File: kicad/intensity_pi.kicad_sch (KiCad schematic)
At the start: 65 parts, among them J1 Input A, J2 Input B / Setpoint, J3 Monitor, J4 Output, J7 select 1, SW1 SW_DPDT_x2, SW2 SW_DPDT_x2, SW3 SW_DPDT_x2, SW4 SW_SP4T, SW5 SW_DPDT_x2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

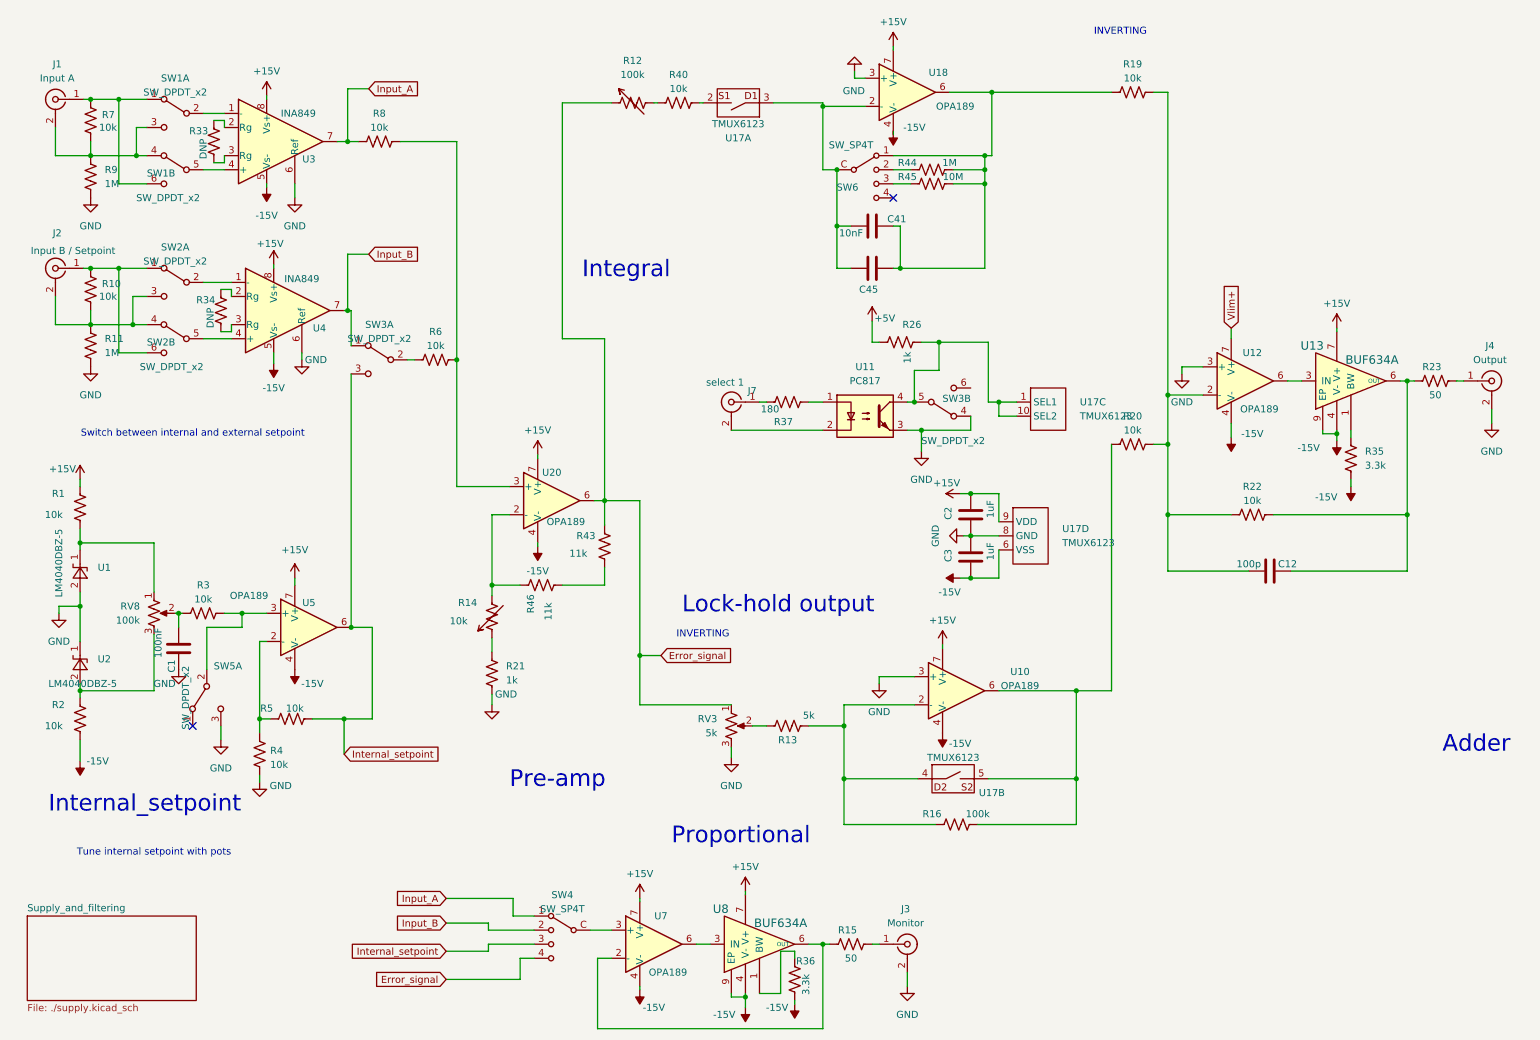
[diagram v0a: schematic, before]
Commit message: Updated Schematic, removed sw1,2,3a,4, have to fix 3a for zero offset switch
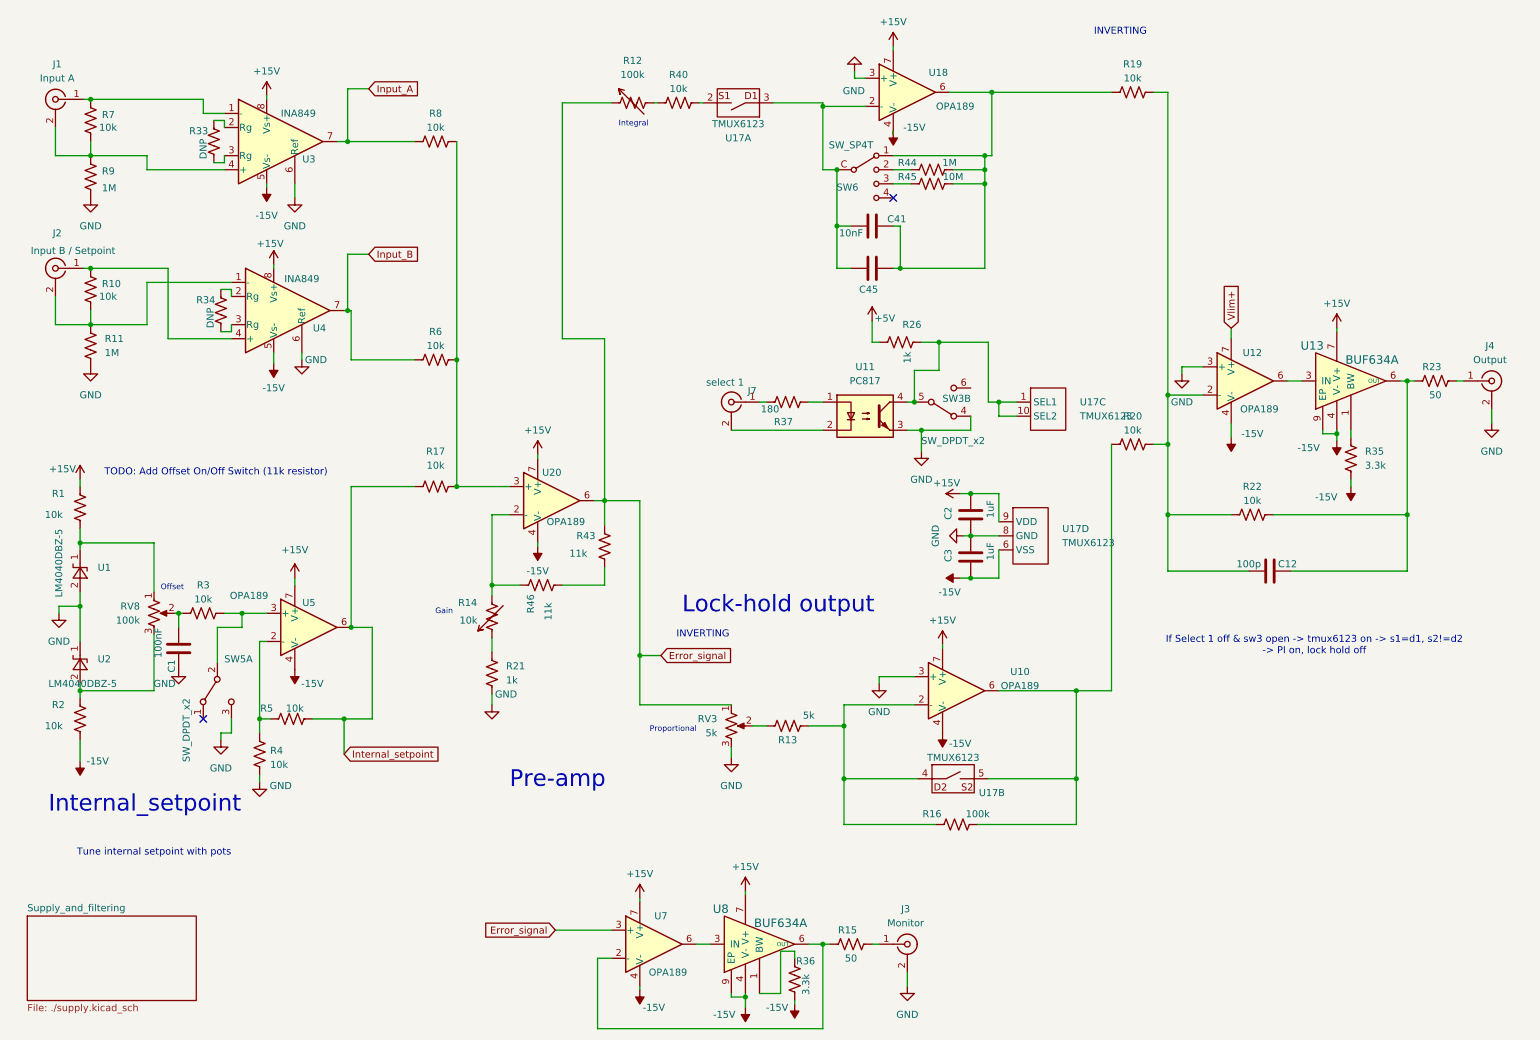
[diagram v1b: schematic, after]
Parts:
- removed SW1, SW2: SW_DPDT_x2, lib:MHS222, symbol local_lib:SW_DPDT_x2
- removed unit 1 of SW3
- removed SW4: SW_SP4T, lib:SLB1470, symbol local_lib:SW_SP4T
- added R17: 10k, symbol Device:R_US
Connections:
- net Error_signal: now also U7.3 (+)
- net Input_B: now also R6.1
- net Internal_setpoint: now also R17.1
- net at U3.1 (-): now also J1.1 (In), R7.2
- net at U3.4 (+): now also J1.2 (Ext), R7.1, R9.2
- net at R6.2, R8.2, U20.3 (+): now also R17.2
- net at J2.1 (In), R10.2: now also U4.4 (+)
- net at U4.1 (-): now also J2.2 (Ext), R10.1, R11.2
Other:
- note added: "Gain"
- note added: "If Select 1 off & sw3 open -> tmux6123 on -> s1=d1, s2!=d2 -> PI on, lock hold off"
- note added: "Offset"
- note added: "TODO: Add Offset On/Off Switch (11k resistor)"
- note removed: "Adder"
- note removed: "Switch between internal and external setpoint"
- moved on the sheet: R8, SW5A

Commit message: Finished Cleaning up Schematic, TODO: Add LED and pick parts
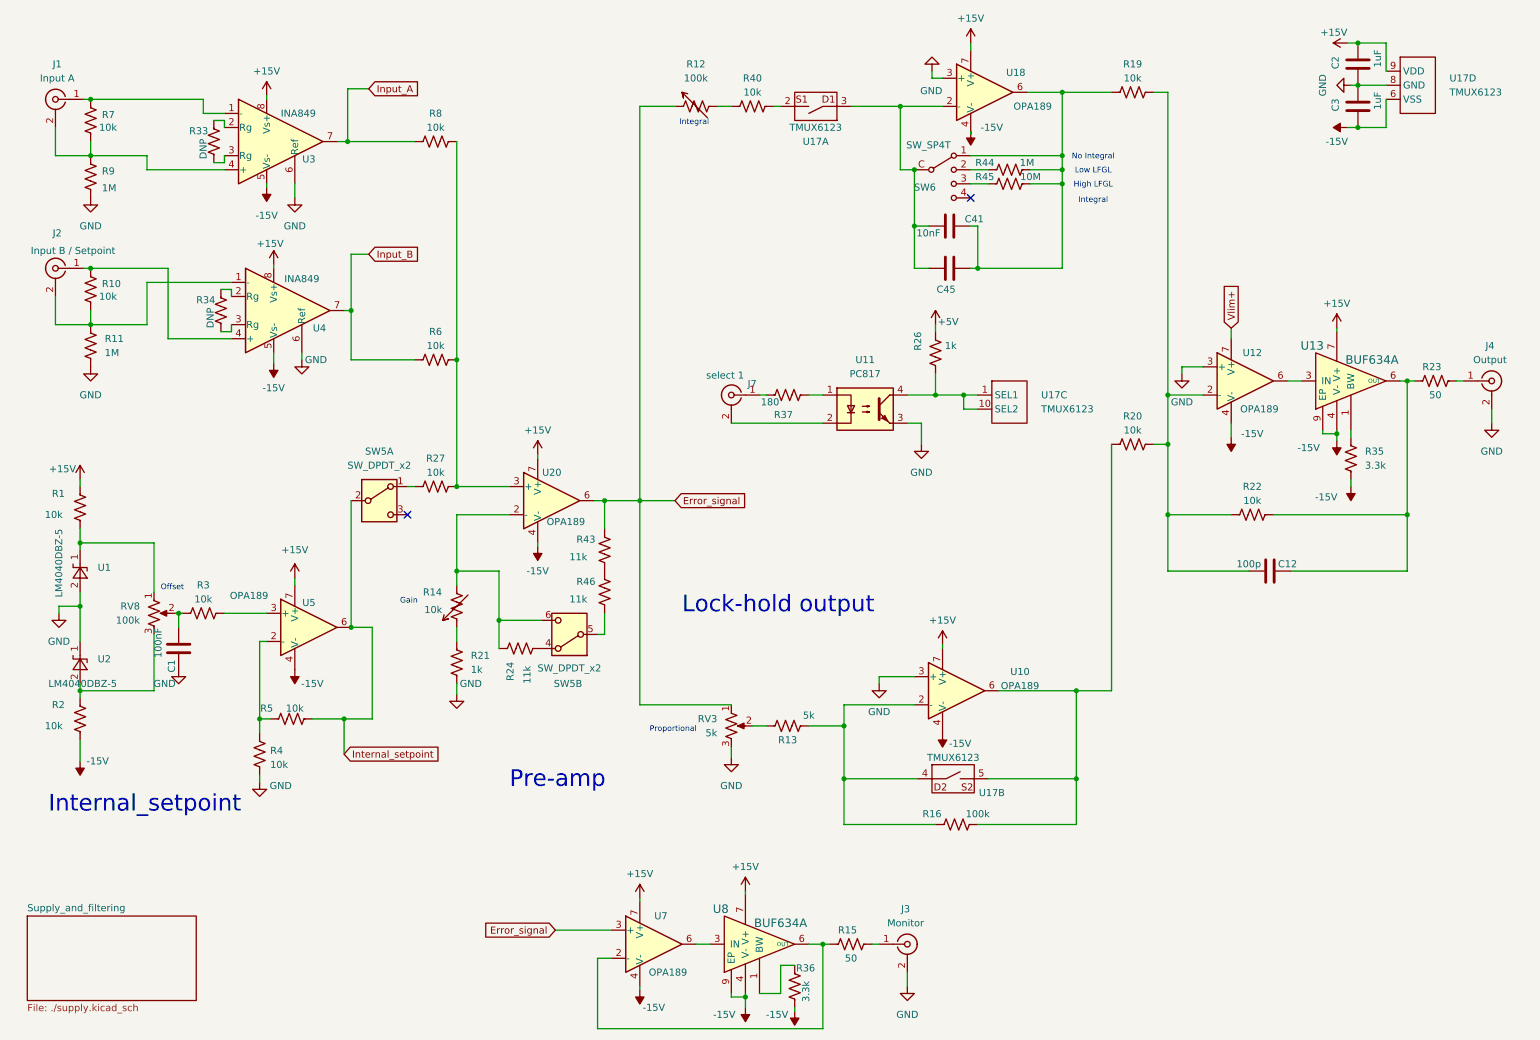
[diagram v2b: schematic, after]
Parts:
- removed R17: 10k, symbol Device:R_US
- removed SW3, SW5: SW_DPDT_x2, lib:MHS222, symbol local_lib:SW_DPDT_x2
- added R24: 11k, Resistor_SMD:R_0805_2012Metric, symbol Device:R_US
- added R27: 10k, Resistor_SMD:R_0805_2012Metric, symbol Device:R_US
- added SW5: SW_DPDT_x2, lib:MHS222, symbol Switch:SW_DPDT_x2
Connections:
- net +5V: now also R26.1; no longer R26.2
- net Internal_setpoint: now also SW5.2 (B)
- net at R6.2, R8.2, U20.3 (+): now also R27.2
- net at R43.1: now also R46.2; no longer R46.1
- net at R14.2, U20.2 (-): now also R24.2, SW5.6 (C); no longer R46.2
- net at U11.4, U17.1 (SEL1), U17.10 (SEL2): now also R26.2; no longer R26.1
- new net: R27.1, SW5.1 (A)
- new net: R24.1, SW5.4 (A)
- new net: R46.1, SW5.5 (B)
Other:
- note added: "High LFGL"
- note added: "Low LFGL"
- note added: "No Integral"
- note removed: "INVERTING"
- note removed: "If Select 1 off & sw3 open -> tmux6123 on -> s1=d1, s2!=d2 -> PI on, lock hold off"
- note removed: "TODO: Add Offset On/Off Switch (11k resistor)"
- note removed: "Tune internal setpoint with pots"
- moved on the sheet: C2, C3, C41, C45, J7, R12, R14, R21, R26, R36, R37, R40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

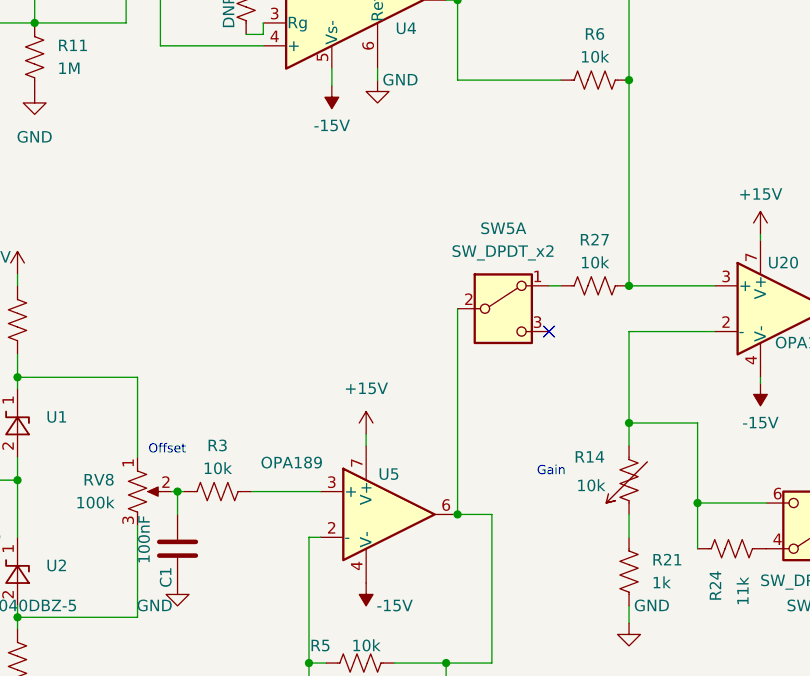
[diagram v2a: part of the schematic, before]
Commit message: Cleaned up PCB, custom footprint for switch
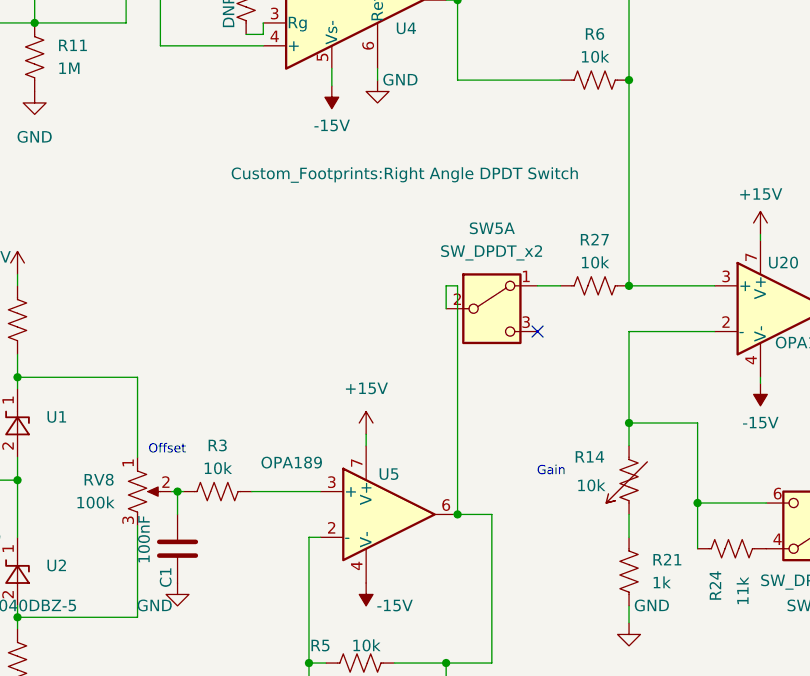
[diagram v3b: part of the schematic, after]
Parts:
- SW5: footprint lib:MHS222 -> Custom_Footprints:Right Angle DPDT Switch
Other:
- moved on the sheet: SW5A
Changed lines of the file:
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@@
 	)
 	(no_connect
-		(at 82.55 104.14)
+		(at 81.28 104.14)
 	)
 	(no_connect
@@
 	(wire
 		(pts
-			(xy 72.39 101.6) (xy 72.39 124.46)
+			(xy 71.12 101.6) (xy 71.12 99.06)
 		)
 		(stroke
@@
 	(wire
 		(pts
+			(xy 72.39 99.06) (xy 72.39 124.46)
+		)
+		(stroke
+			(width 0)
+			(type default)
+		)
+	)
+	(wire
+		(pts
 			(xy 55.88 127) (xy 55.88 140.97)
 		)
@@
 	(wire
 		(pts
+			(xy 71.12 99.06) (xy 72.39 99.06)
+		)
+		(stroke
+			(width 0)
+			(type default)
+		)
+	)
+	(wire
+		(pts
 			(xy 58.42 76.835) (xy 58.42 74.93)
 		)
@@
 	(wire
 		(pts
-			(xy 82.55 99.06) (xy 83.82 99.06)
+			(xy 81.28 99.06) (xy 83.82 99.06)
 		)
 		(stroke
@@
 	(symbol
 		(lib_id "Switch:SW_DPDT_x2")
-		(at 77.47 101.6 0)
+		(at 76.2 101.6 0)
 		(unit 1)
 		(exclude_from_sim no)
@@
 		(on_board yes)
 		(dnp no)
-		(fields_autoplaced yes)
 		(property "Reference" "SW5"
-			(at 77.47 92.71 0)
+			(at 76.2 92.71 0)
 			(effects
 				(font
@@
 		)
 		(property "Value" "SW_DPDT_x2"
-			(at 77.47 95.25 0)
+			(at 76.2 95.25 0)
 			(effects
 				(font
@@
 			)
 		)
-		(property "Footprint" "lib:MHS222"
-			(at 77.47 101.6 0)
+		(property "Footprint" "Custom_Footprints:Right Angle DPDT Switch"
+			(at 66.548 86.614 0)
 			(effects
 				(font
 					(size 1.27 1.27)
 				)
-				(hide yes)
 			)
 		)
 		(property "Datasheet" "~"
-			(at 77.47 101.6 0)
+			(at 76.2 101.6 0)
 			(effects
 				(font
@@
 		)
 		(property "Description" "Switch, dual pole double throw, separate symbols"
-			(at 77.47 101.6 0)
+			(at 76.2 101.6 0)
 			(effects
 				(font
@@
 		)
 		(property "DIGIKEY" "EG2404-ND"
-			(at 77.47 101.6 0)
+			(at 76.2 101.6 0)
 			(effects
 				(font
@@
 		)
 		(property "PARTNO" "100DP1T2B4M6QE"
-			(at 77.47 101.6 0)
+			(at 76.2 101.6 0)
 			(effects
 				(font
@@
 			)
 		)
-		(property "Footprint" "lib:MHS222"
+		(property "Footprint" "Custom_Footprints:Right Angle DPDT Switch"
 			(at 111.76 125.73 0)
 			(effects
